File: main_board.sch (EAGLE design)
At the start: 42 parts, among them J1 TBL009-254-02GY-2GY, J2 709176001501006, J3 709176001501006, J4 709176001501006, U1 MAX9019EKA+T, U2 AEM10941-QFN

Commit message: timer implemented in schematic
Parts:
- added C10, C11, C9: 0.1uF, MF_Passives:CAPACITOR_NP_0603
- added J5: MF-CON-2.54mm-01x02, MF_Connectors:CON_01X02_PTH_2.54MM
- added R27, R28: 100K, MF_Passives:RESISTOR_0805
- added R29: 162K, MF_Passives:RESISTOR_0805
- added R30: 121K, MF_Passives:RESISTOR_0805
- added SW1, SW2: (no value), MF_Switches:TACT_4.2MM
- added TP1, TP2, TP3, TP4, TP5, TP6: 5115, PP_Connectors:TEST_POINT_SINGLE_KEYSTONE_5115-5119
- added U3: LTC2956IMS-1#PBF, PP_DigitalIC:LTC2956IMS-1#PBF
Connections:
- new net !OFFALERT: U3.!OFFALERT
- new net !ONALERT: U3.!ONALERT
- new net !PB: SW1.P$4, U3.!PB
- new net !PBOUT: U3.!PBOUT
- new net !SLEEP: C10.P$1, R27.P$2, SW2.P$1, U3.!SLEEP
- new net EN: U3.EN
- new net LONG: R28.P$1, U3.LONG
- new net PERIOD: R30.P$2, U3.PERIOD
- new net RANGE: R28.P$2, R29.P$2, U3.RANGE
- net !OUT: now also TP6.P$1
- net 3.3V: now also C11.P$1, C9.P$1, J5.PIN1, SW2.P$4, U3.VCC
- net BATT: now also TP3.P$1
- net GND: now also C10.P$2, C11.P$2, C9.P$2, R27.P$1, R29.P$1, R30.P$1, SW1.P$1, TP2.P$1, U3.GND, U3.ONMAX
- net HVOUT: now also J5.PIN2, TP4.P$1
- net OUT: now also TP5.P$1
- net SOLAR_+V: now also TP1.P$1
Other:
- moved on the sheet: C1, C2, C3, C4, C5, C6, C7, C8, J1, J2, J3, J4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

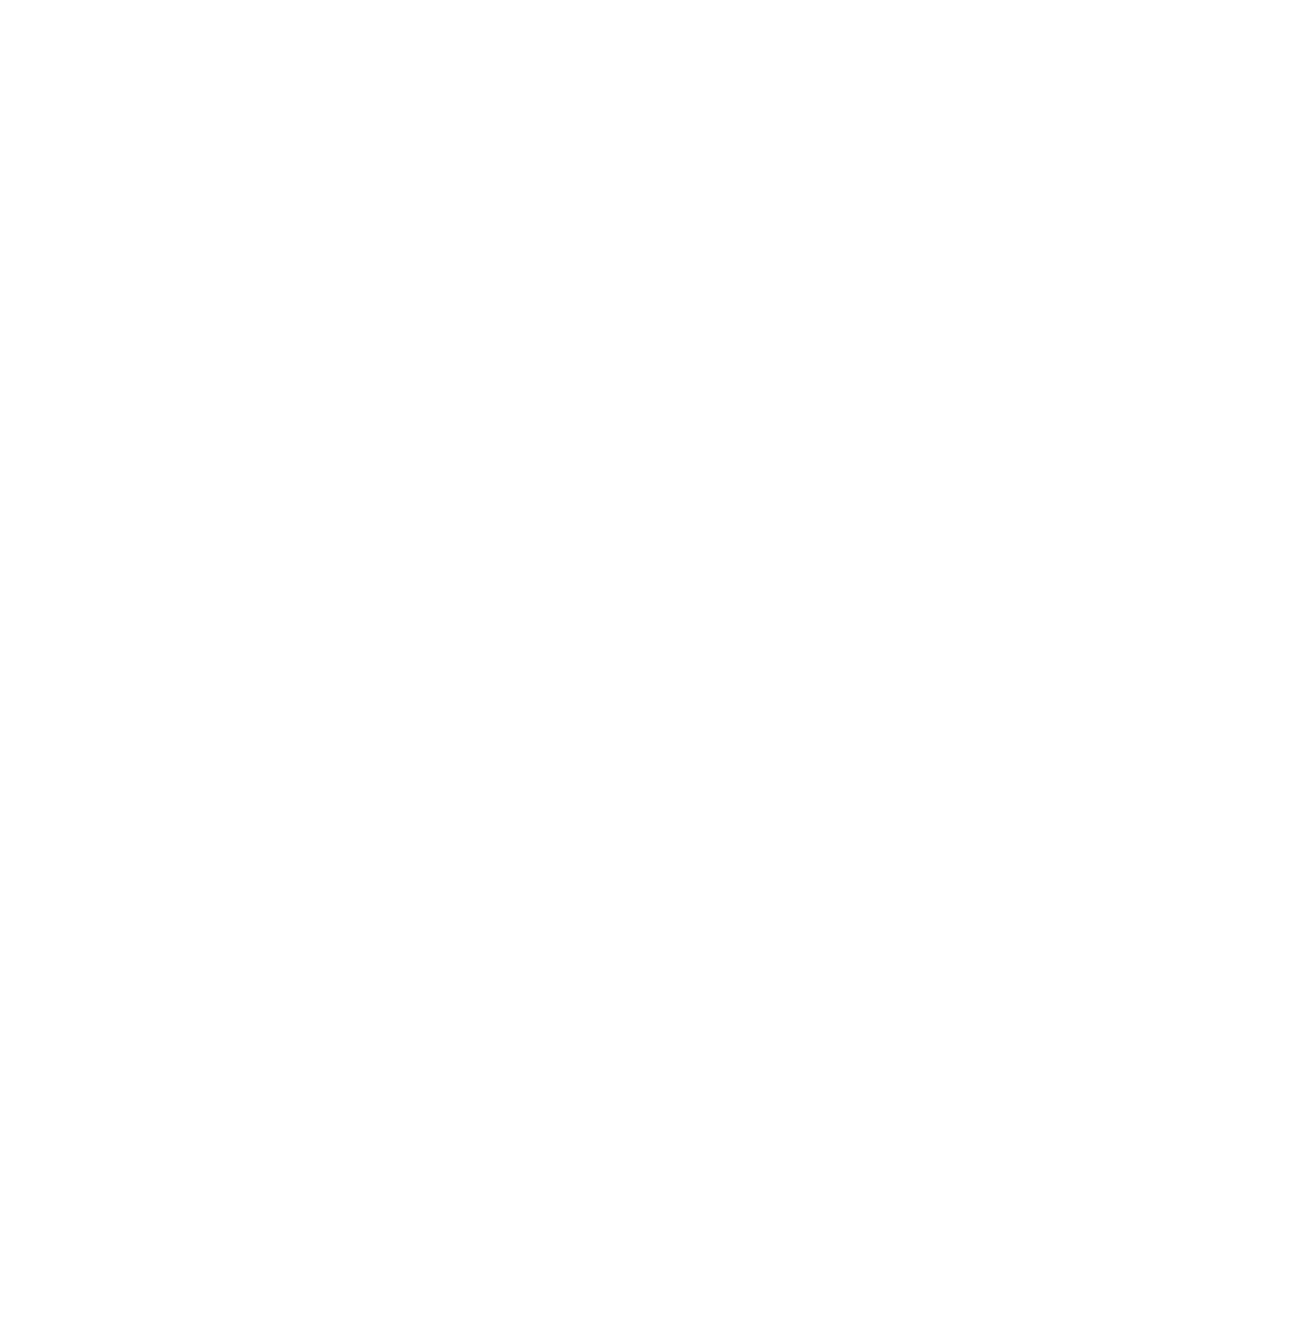
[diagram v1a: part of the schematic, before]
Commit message: Added analog switch
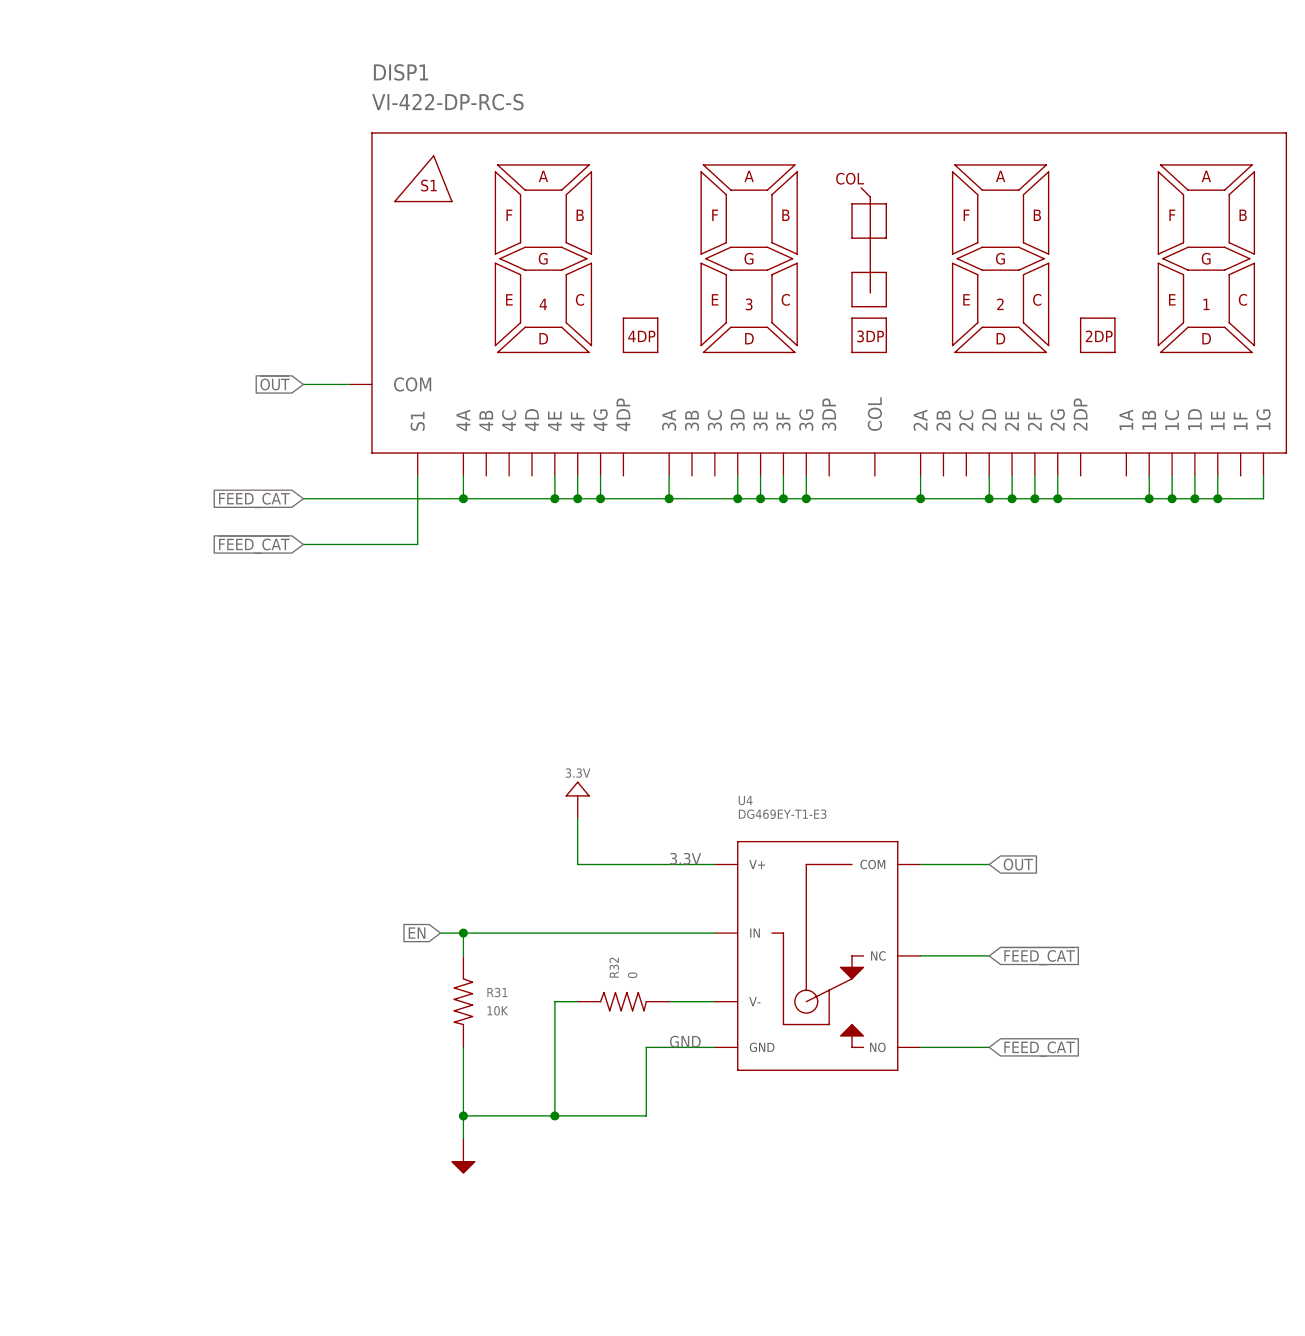
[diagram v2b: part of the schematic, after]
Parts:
- added DISP1: VI-422-DP-RC-S, PP_Displays:VI-422-DP-RC-S
- added R31: 10K, MF_Passives:RESISTOR_0805
- added R32: 0, MF_Passives:RESISTOR_0805
- added U4: DG469EY-T1-E3, PP_AnalogIC:DG469EY-T1-E3
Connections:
- new net !FEED_CAT: DISP1.S1, U4.NC
- new net FEED_CAT: DISP1.1B, DISP1.1C, DISP1.1D, DISP1.1E, DISP1.1G, DISP1.2A, DISP1.2D, DISP1.2E, DISP1.2F, DISP1.2G, DISP1.3A, DISP1.3D, DISP1.3E, DISP1.3F, DISP1.3G, DISP1.4A, DISP1.4E, DISP1.4F, DISP1.4G, U4.NO
- new net N$4: R32.P$2, U4.V-
- net !OUT: now also DISP1.COM
- net 3.3V: now also U4.V+
- net EN: now also R31.P$1, U4.IN
- net GND: now also R31.P$2, R32.P$1, U4.GND
- net OUT: now also U4.COM
